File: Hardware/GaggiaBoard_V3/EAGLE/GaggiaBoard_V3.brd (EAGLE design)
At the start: 45 x 100 mm, 75 parts, among them IC1 LD117AS33TR, J1 4PIN, J10 PIN262409-1, J11 PIN262409-1, J12 PIN262409-1, J13 PIN262409-1, J2 Vertical Qwiic Connector, J27 6PIN, J5 2PIN, J6 3PIN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

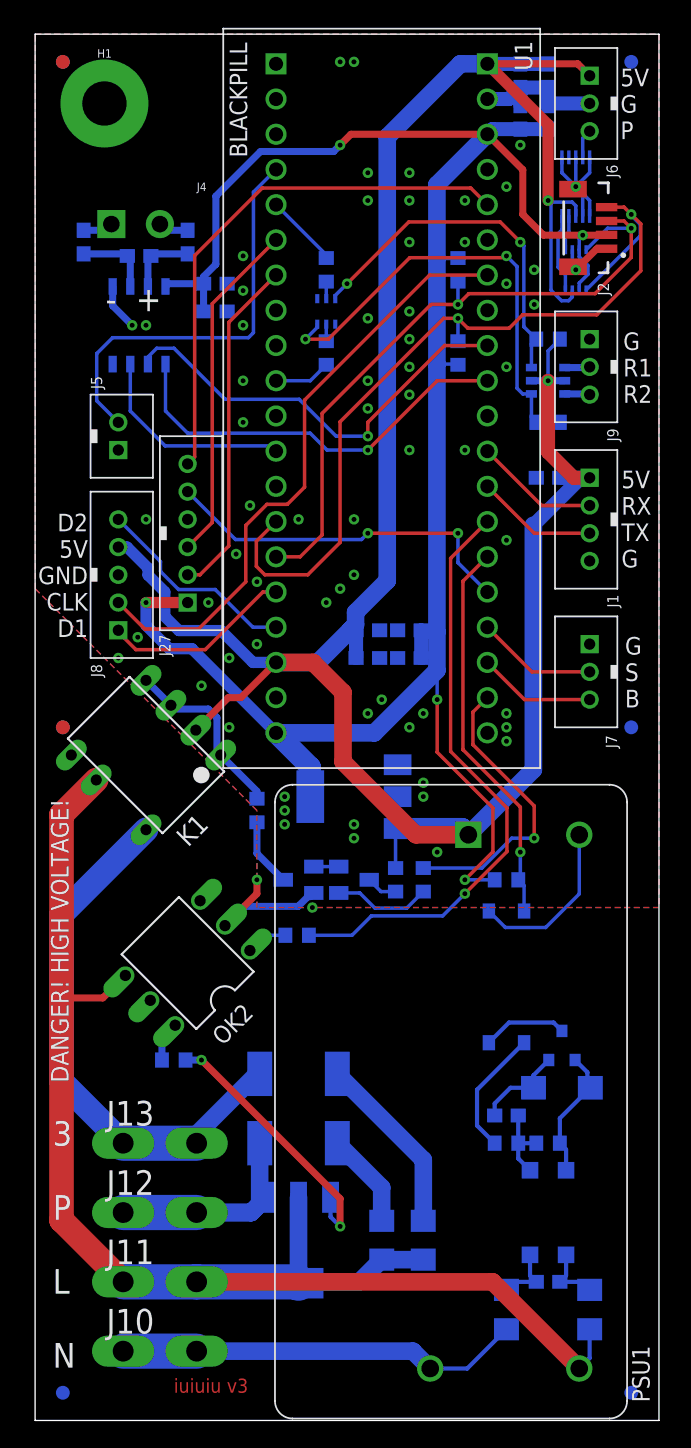
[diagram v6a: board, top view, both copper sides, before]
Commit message: Faston drill fix
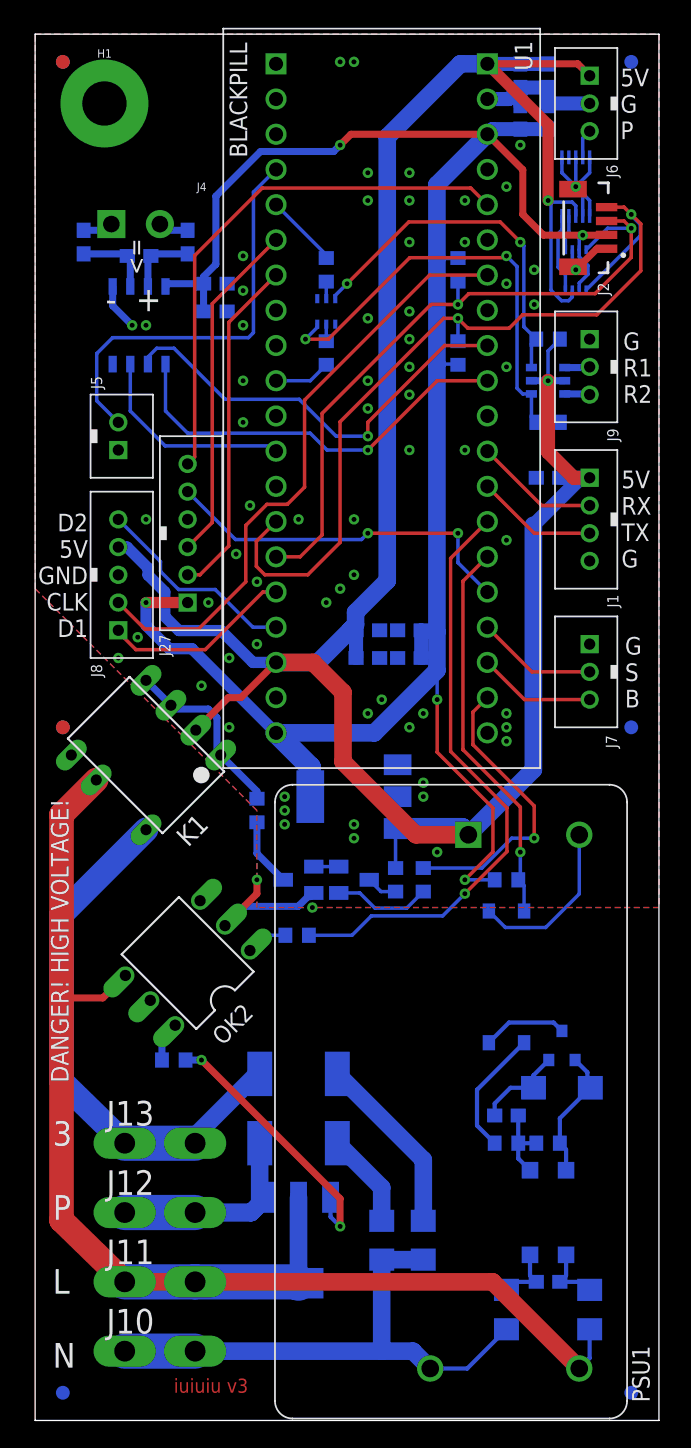
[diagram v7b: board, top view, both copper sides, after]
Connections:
- net AC_N: now also C16.1, C5.1
- net AC_P: no longer C16.1, C5.1
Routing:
- net AC_N: track 29.3 -> 38.8 mm
- net AC_P: track 106.3 -> 101.7 mm
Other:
- board text added: "<="
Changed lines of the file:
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@@
 RX
 3V3</text>
+<text x="7.239" y="83.947" size="1.27" layer="21" rot="R90" align="center">&lt;=</text>
 </plain>
 <attributes>
@@
 <attribute name="VALUE" x="24.3208" y="47.54" size="1.27" layer="28" rot="MR270"/>
 </element>
-<element name="J13" library="con-faston" library_urn="urn:adsk.eagle:library:144" package="62409-1" package3d_urn="urn:adsk.eagle:package:6760/1" override_package3d_urn="urn:adsk.eagle:package:36461343/2" override_package_urn="urn:adsk.eagle:footprint:6751/1" value="PIN262409-1" x="9" y="20" smashed="yes">
+<element name="J13" library="con-faston" package="62409-1" package3d_urn="urn:adsk.eagle:package:39428999/1" override_package3d_urn="urn:adsk.eagle:package:36461343/2" override_package_urn="urn:adsk.eagle:footprint:6751/1" override_locally_modified="yes" value="PIN262409-1" x="9" y="20" smashed="yes">
 <attribute name="LCSC" value="C86495" x="57.26" y="-60.01" size="1.778" layer="27" display="off"/>
 <attribute name="MF" value="" x="57.26" y="-60.01" size="1.778" layer="27" display="off"/>
@@
 <attribute name="VALUE" x="5.15" y="16.19" size="1.778" layer="27"/>
 </element>
-<element name="J12" library="con-faston" library_urn="urn:adsk.eagle:library:144" package="62409-1" package3d_urn="urn:adsk.eagle:package:6760/1" override_package3d_urn="urn:adsk.eagle:package:36461344/2" override_package_urn="urn:adsk.eagle:footprint:6751/1" value="PIN262409-1" x="9" y="15" smashed="yes">
+<element name="J12" library="con-faston" package="62409-1" package3d_urn="urn:adsk.eagle:package:39428999/1" override_package3d_urn="urn:adsk.eagle:package:36461344/2" override_package_urn="urn:adsk.eagle:footprint:6751/1" override_locally_modified="yes" value="PIN262409-1" x="9" y="15" smashed="yes">
 <attribute name="LCSC" value="C86495" x="75.04" y="-65.01" size="1.778" layer="27" display="off"/>
 <attribute name="MF" value="" x="75.04" y="-65.01" size="1.778" layer="27" display="off"/>
@@
 <attribute name="VALUE" x="5.15" y="11.19" size="1.778" layer="27"/>
 </element>
-<element name="J10" library="con-faston" library_urn="urn:adsk.eagle:library:144" package="62409-1" package3d_urn="urn:adsk.eagle:package:6760/1" override_package3d_urn="urn:adsk.eagle:package:36461296/2" override_package_urn="urn:adsk.eagle:footprint:6751/1" value="PIN262409-1" x="9" y="5" smashed="yes">
+<element name="J10" library="con-faston" package="62409-1" package3d_urn="urn:adsk.eagle:package:39428999/1" override_package3d_urn="urn:adsk.eagle:package:36461296/2" override_package_urn="urn:adsk.eagle:footprint:6751/1" override_locally_modified="yes" value="PIN262409-1" x="9" y="5" smashed="yes">
 <attribute name="LCSC" value="C86495" x="92.82" y="-75.01" size="1.778" layer="27" display="off"/>
 <attribute name="MF" value="" x="92.82" y="-75.01" size="1.778" layer="27" display="off"/>
@@
 <attribute name="VALUE" x="43.29633125" y="86.016" size="0.6096" layer="27" rot="R90"/>
 </element>
-<element name="J11" library="con-faston" library_urn="urn:adsk.eagle:library:144" package="62409-1" package3d_urn="urn:adsk.eagle:package:6760/1" override_package3d_urn="urn:adsk.eagle:package:36461311/2" override_package_urn="urn:adsk.eagle:footprint:6751/1" value="PIN262409-1" x="9" y="10" smashed="yes">
+<element name="J11" library="con-faston" package="62409-1" package3d_urn="urn:adsk.eagle:package:39428999/1" override_package3d_urn="urn:adsk.eagle:package:36461311/2" override_package_urn="urn:adsk.eagle:footprint:6751/1" override_locally_modified="yes" value="PIN262409-1" x="9" y="10" smashed="yes">
 <attribute name="LCSC" value="C86495" x="34.4" y="-78.9" size="1.778" layer="27" display="off"/>
 <attribute name="MF" value="" x="34.4" y="-78.9" size="1.778" layer="27" display="off"/>
@@
 <wire x1="34" y1="6.578" x2="31.172" y2="3.75" width="0.3048" layer="16"/>
 <wire x1="31.172" y1="3.75" x2="28.5" y2="3.75" width="0.3048" layer="16"/>
-<wire x1="6.35" y1="5" x2="11.65" y2="5" width="2.54" layer="16"/>
+<wire x1="6.46" y1="5" x2="11.54" y2="5" width="2.54" layer="16"/>
 <wire x1="28.5" y1="3.75" x2="27.25" y2="5" width="1.27" layer="16"/>
-<wire x1="27.25" y1="5" x2="11.65" y2="5" width="1.27" layer="16"/>
+<wire x1="27.25" y1="5" x2="25.019" y2="5" width="1.27" layer="16"/>
+<contactref element="C5" pad="1"/>
+<contactref element="C16" pad="1"/>
+<wire x1="25.019" y1="5" x2="11.54" y2="5" width="1.27" layer="16"/>
+<wire x1="25" y1="11.6" x2="25" y2="5.019" width="1.27" layer="16"/>
+<wire x1="25" y1="5.019" x2="25.019" y2="5" width="1.27" layer="16"/>
+<wire x1="28" y1="11.6" x2="25" y2="11.6" width="1.27" layer="16"/>
 </signal>
 <signal name="AC_P">
 <contactref element="TR1" pad="2"/>
 <contactref element="TR1" pad="4"/>
-<contactref element="OK2" pad="4"/>
 <contactref element="R20" pad="1"/>
 <contactref element="PSU1" pad="AC/L"/>
@@
 <wire x1="40" y1="6.578" x2="40" y2="4.5" width="0.3048" layer="16"/>
 <wire x1="40" y1="4.5" x2="39.25" y2="3.75" width="0.3048" layer="16"/>
-<wire x1="6.35" y1="10" x2="11.65" y2="10" width="2.54" layer="16"/>
-<wire x1="11.65" y1="10" x2="18.901" y2="10" width="2.54" layer="16"/>
+<wire x1="6.46" y1="10" x2="11.54" y2="10" width="2.54" layer="16"/>
+<wire x1="11.54" y1="10" x2="18.901" y2="10" width="2.54" layer="16"/>
 <wire x1="18.901" y1="10" x2="19" y2="9.901" width="2.54" layer="16"/>
 <wire x1="19" y1="16.099" x2="19" y2="10.099" width="1.27" layer="16"/>
 <wire x1="19" y1="10.099" x2="18.901" y2="10" width="1.27" layer="16"/>
-<wire x1="6.35" y1="10" x2="1.905" y2="14.445" width="1.778" layer="1"/>
+<wire x1="6.46" y1="10" x2="1.905" y2="14.445" width="1.778" layer="1"/>
 <wire x1="1.905" y1="43.70105" x2="4.407896875" y2="46.203946875" width="1.778" layer="1"/>
 <wire x1="1.905" y1="14.445" x2="1.905" y2="30.48" width="1.778" layer="1"/>
 <wire x1="1.905" y1="30.48" x2="1.905" y2="43.70105" width="1.778" layer="1"/>
-<wire x1="6.509871875" y1="32.101971875" x2="4.8879" y2="30.48" width="0.508" layer="1"/>
 <wire x1="4.8879" y1="30.48" x2="1.905" y2="30.48" width="0.508" layer="1"/>
 <wire x1="39.25" y1="3.75" x2="33" y2="10" width="1.27" layer="1"/>
-<wire x1="33" y1="10" x2="11.65" y2="10" width="1.27" layer="1"/>
-<contactref element="C5" pad="1"/>
-<contactref element="C16" pad="1"/>
-<wire x1="25" y1="11.6" x2="23.4" y2="10" width="1.27" layer="16"/>
-<wire x1="23.4" y1="10" x2="18.901" y2="10" width="1.27" layer="16"/>
-<wire x1="28" y1="11.6" x2="25" y2="11.6" width="1.27" layer="16"/>
+<wire x1="33" y1="10" x2="11.54" y2="10" width="1.27" layer="1"/>
+<contactref element="OK2" pad="4"/>
+<wire x1="6.509871875" y1="32.101971875" x2="4.8879" y2="30.48" width="0.508" layer="1"/>
+<wire x1="6.46" y1="10" x2="11.54" y2="10" width="1.27" layer="1"/>
 </signal>
 <signal name="3WAY">
@@
 <contactref element="J13" pad="A2"/>
 <contactref element="K1" pad="8"/>
-<wire x1="6.35" y1="20" x2="11.65" y2="20" width="2.54" layer="16"/>
-<wire x1="6.35" y1="20" x2="1.905" y2="24.445" width="1.778" layer="16"/>
+<wire x1="6.46" y1="20" x2="11.54" y2="20" width="2.54" layer="16"/>
+<wire x1="6.46" y1="20" x2="1.905" y2="24.445" width="1.778" layer="16"/>
 <wire x1="1.905" y1="36.51684375" x2="8" y2="42.61184375" width="1.778" layer="16"/>
 <wire x1="1.905" y1="24.445" x2="1.905" y2="36.51684375" width="1.778" layer="16"/>
@@
 <wire x1="16.2" y1="25" x2="16.015" y2="25" width="1.27" layer="16"/>
 <wire x1="16.015" y1="25" x2="11.65" y2="20.635" width="1.27" layer="16"/>
-<wire x1="11.65" y1="20.635" x2="11.65" y2="20" width="1.27" layer="16"/>
+<wire x1="11.65" y1="20.635" x2="11.54" y2="20" width="1.27" layer="16"/>
 </signal>
 <signal name="N$8">
@@
 <contactref element="J12" pad="A2"/>
 <contactref element="TR1" pad="1"/>
-<wire x1="6.35" y1="15" x2="11.65" y2="15" width="2.54" layer="16"/>
-<wire x1="11.65" y1="15" x2="15.59" y2="15" width="1.27" layer="16"/>
+<wire x1="6.46" y1="15" x2="11.54" y2="15" width="2.54" layer="16"/>
+<wire x1="11.54" y1="15" x2="15.59" y2="15" width="1.27" layer="16"/>
 <wire x1="15.59" y1="15" x2="16.689" y2="16.099" width="1.27" layer="16"/>
 <contactref element="R13" pad="2"/>
 <wire x1="16.2" y1="20" x2="16.2" y2="15.613" width="1.27" layer="16"/>
 <wire x1="16.2" y1="15.613" x2="15.587" y2="15" width="1.27" layer="16"/>
-<wire x1="15.587" y1="15" x2="11.65" y2="15" width="1.27" layer="16"/>
+<wire x1="15.587" y1="15" x2="11.54" y2="15" width="1.27" layer="16"/>
 </signal>
 <signal name="N$39">

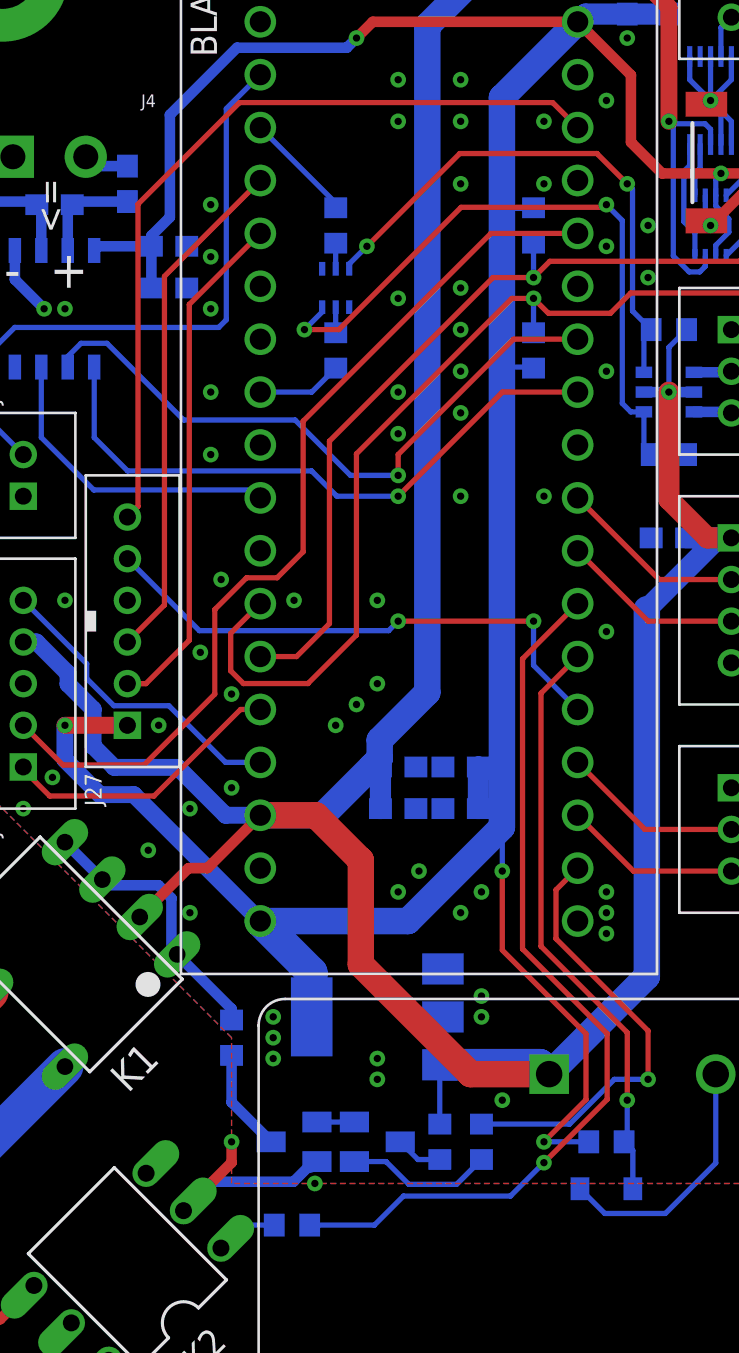
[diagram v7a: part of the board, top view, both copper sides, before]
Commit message: pull downs on GPIO outputs
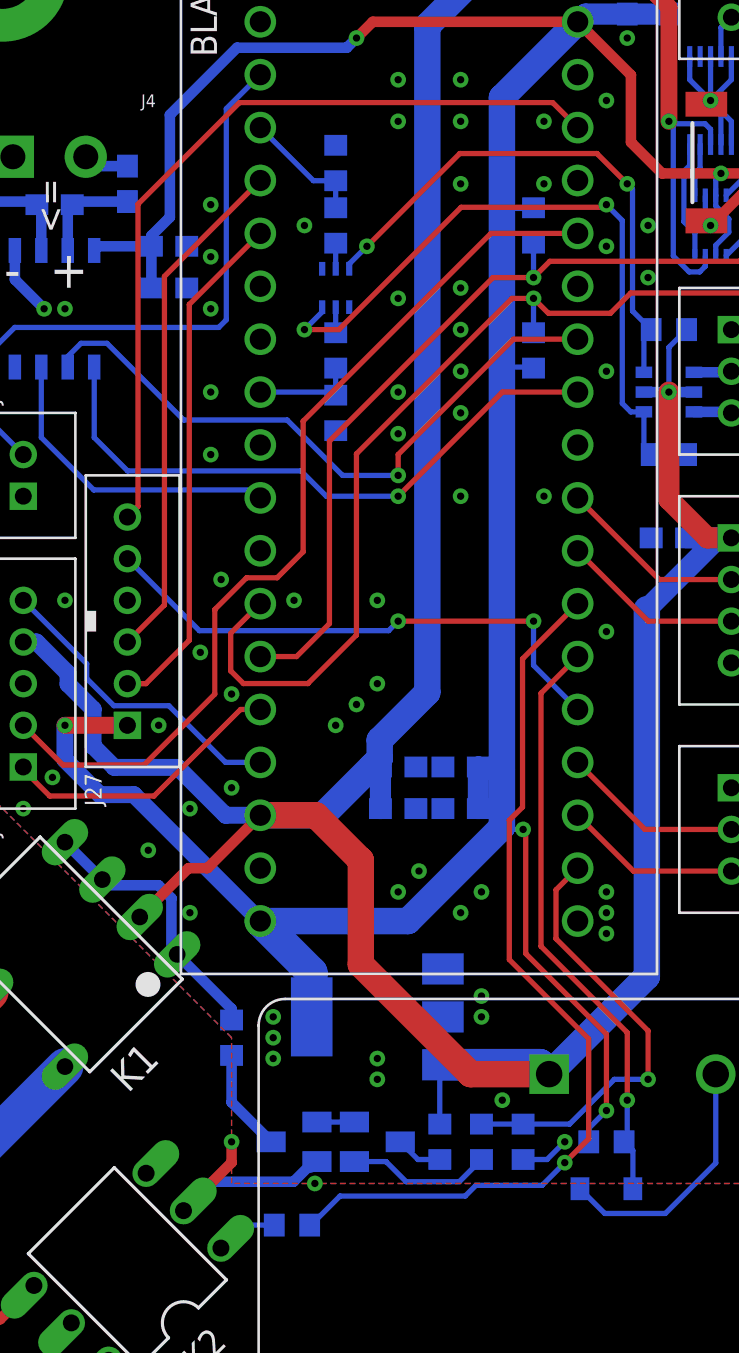
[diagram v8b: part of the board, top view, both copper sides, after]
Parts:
- added R6, R7, R9: 3K3, rcl:R0603
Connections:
- net GND: now also R6.1, R7.1, R9.1
- net PA15: now also R6.2
- net PA8: now also R7.2
- net PC13: now also R9.2
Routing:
- net GND: track 54.1 -> 56.5 mm, vias 67 -> 69
- net 3V3: track 158.1 -> 156.4 mm
- net PA15: track 4.10 -> 4.98 mm
- net PA8: track 5.35 -> 5.98 mm
